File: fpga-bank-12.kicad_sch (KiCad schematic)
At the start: 1 part

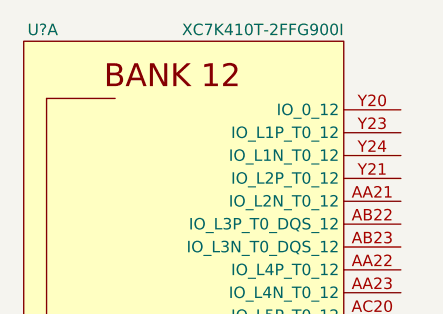
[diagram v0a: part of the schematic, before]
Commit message: Fix FPGA symbol
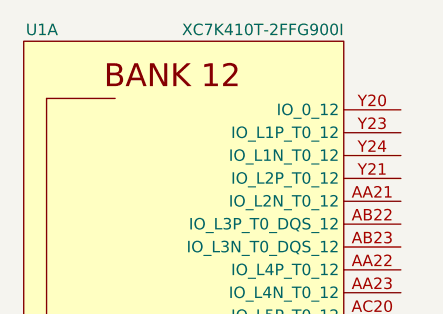
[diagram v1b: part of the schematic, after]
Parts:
- gave numbers to parts that had none: 1
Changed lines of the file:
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@@
     (effects (font (size 1.27 1.27)) (justify left))
   )
-  (symbol (lib_name "XC7K410T-2FFG900I_1") (lib_id "antmicroMicrocontrollers:XC7K410T-2FFG900I") (at 119.38 144.78 0) (unit 1)
+  (symbol (lib_id "antmicroMicrocontrollers:XC7K410T-2FFG900I") (at 119.38 144.78 0) (unit 1)
     (in_bom yes) (on_board yes)
-    (property "Reference" "U?" (id 0) (at 105.41 74.93 0)
+    (property "Reference" "U1" (id 0) (at 105.41 74.93 0)
       (effects (font (size 1.27 1.27)) (justify right))
     )

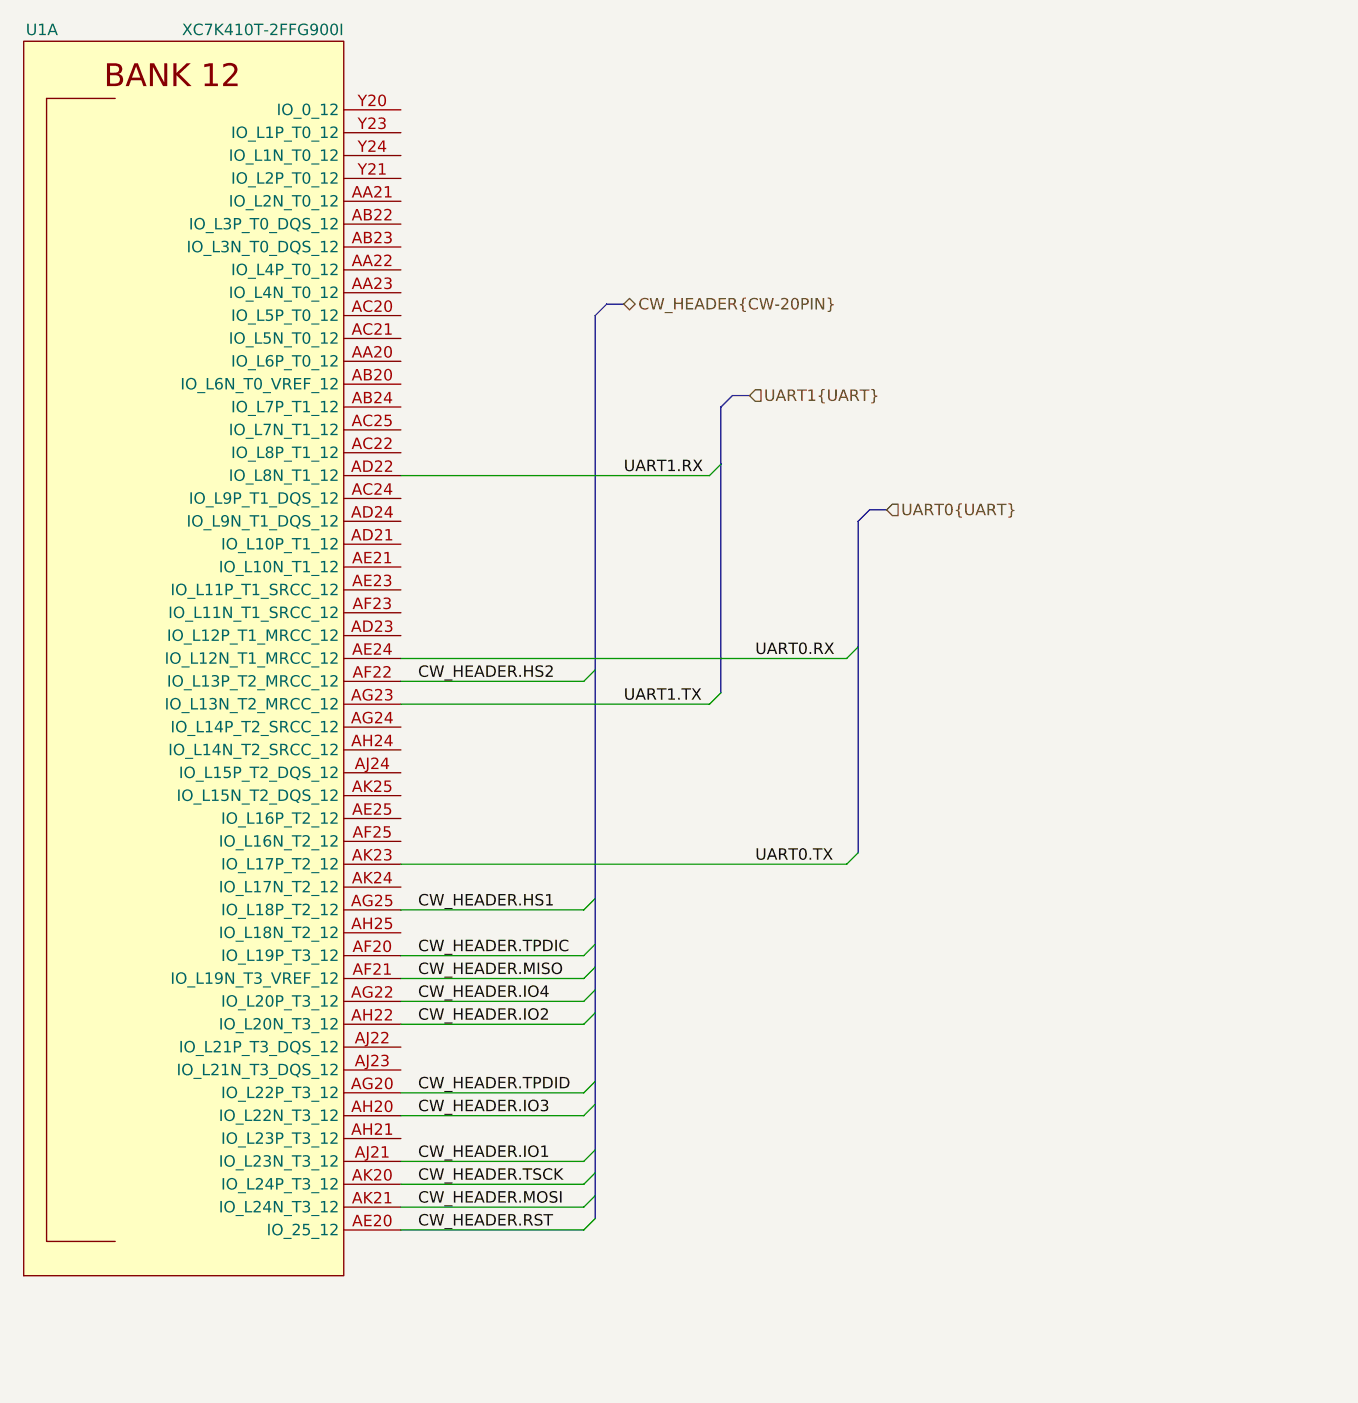
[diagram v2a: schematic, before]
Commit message: Add new pinout to sup MCU. Start connecting it to FPGA
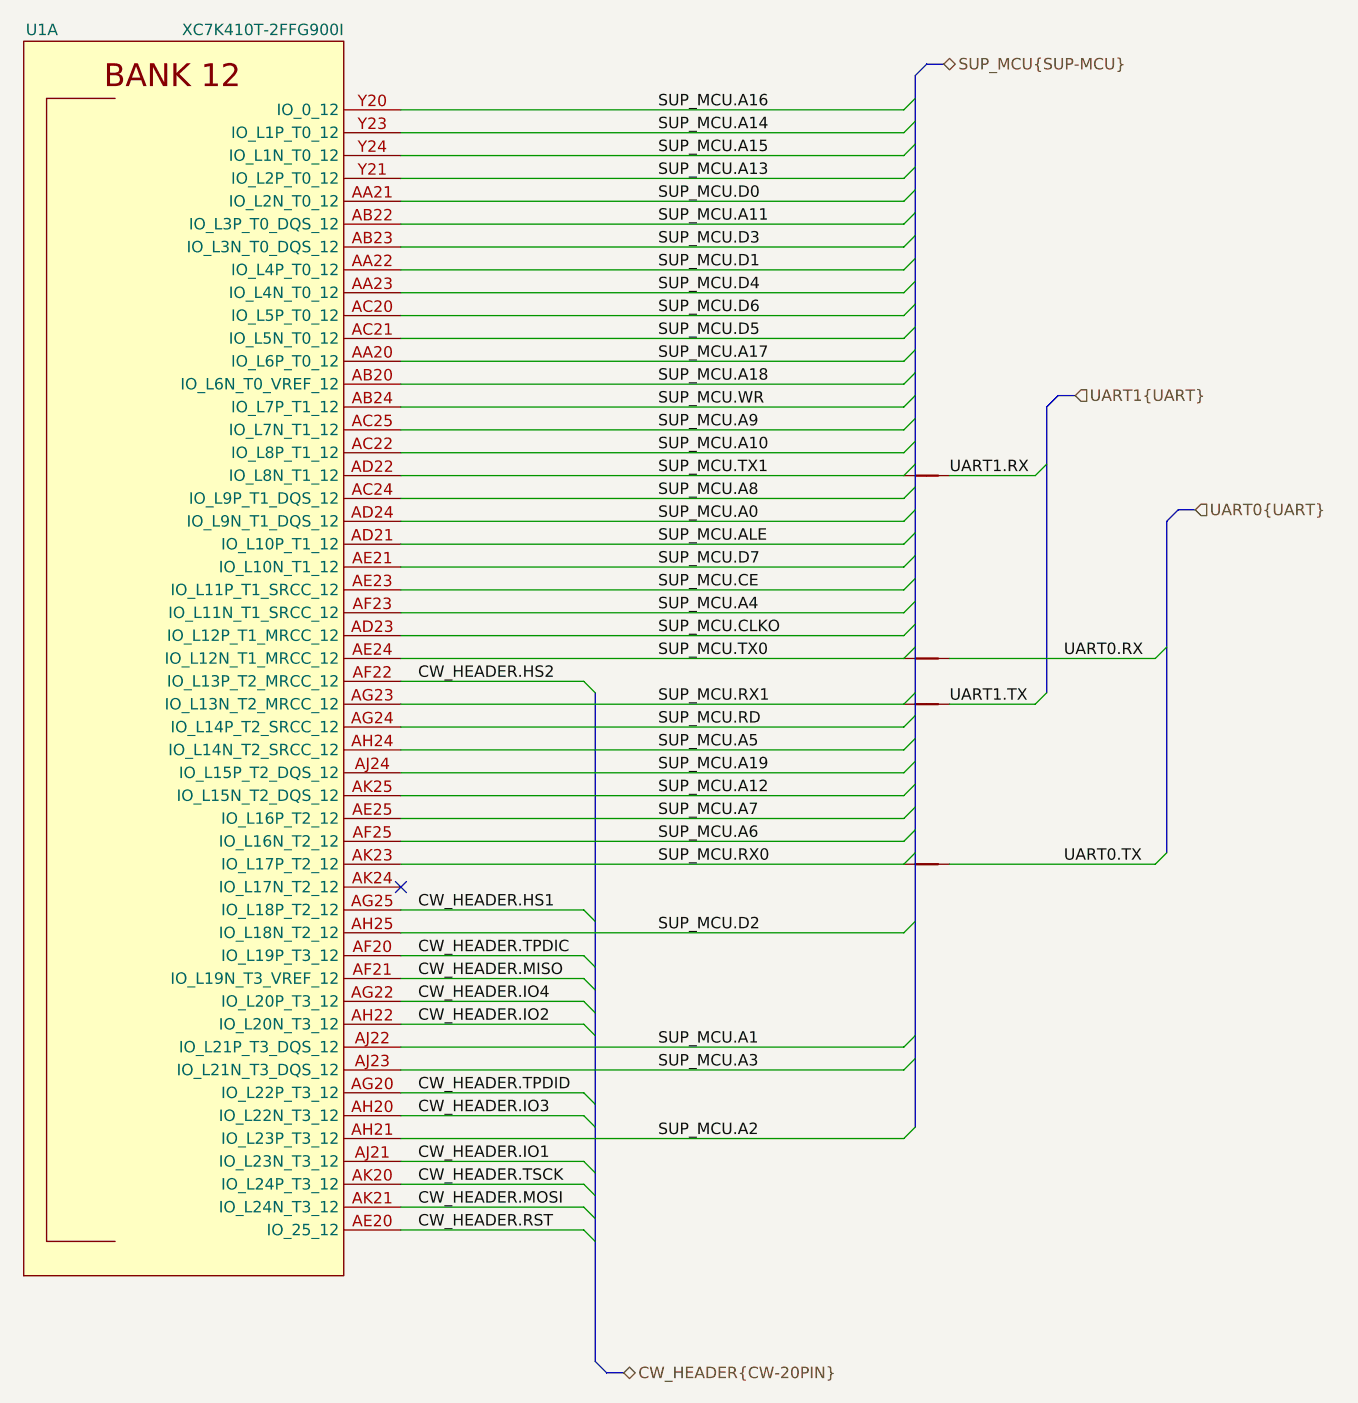
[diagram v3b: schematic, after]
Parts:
- added NT? (x4): NetTie_2, antmicro-footprints:NetTie-2_SMD_Pad0.127mm, symbol antmicroShuntsJumpers:NetTie_2
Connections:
- net UART0.RX: now also NT?.2; no longer U1.AE24 (IO_L12N_T1_MRCC_12)
- net UART0.TX: now also NT?.2; no longer U1.AK23 (IO_L17P_T2_12)
- net UART1.RX: now also NT?.2; no longer U1.AD22 (IO_L8N_T1_12)
- net UART1.TX: now also NT?.2; no longer U1.AG23 (IO_L13N_T2_MRCC_12)
- net SUP_MCU.A17: now reaches U1.AA20 (IO_L6P_T0_12)
- net SUP_MCU.D0: now reaches U1.AA21 (IO_L2N_T0_12)
- net SUP_MCU.D1: now reaches U1.AA22 (IO_L4P_T0_12)
- net SUP_MCU.D4: now reaches U1.AA23 (IO_L4N_T0_12)
- net SUP_MCU.A18: now reaches U1.AB20 (IO_L6N_T0_VREF_12)
- net SUP_MCU.A11: now reaches U1.AB22 (IO_L3P_T0_DQS_12)
- net SUP_MCU.D3: now reaches U1.AB23 (IO_L3N_T0_DQS_12)
- net SUP_MCU.WR: now reaches U1.AB24 (IO_L7P_T1_12)
- net SUP_MCU.D6: now reaches U1.AC20 (IO_L5P_T0_12)
- net SUP_MCU.D5: now reaches U1.AC21 (IO_L5N_T0_12)
- net SUP_MCU.A10: now reaches U1.AC22 (IO_L8P_T1_12)
- net SUP_MCU.A8: now reaches U1.AC24 (IO_L9P_T1_DQS_12)
- net SUP_MCU.A9: now reaches U1.AC25 (IO_L7N_T1_12)
- net SUP_MCU.ALE: now reaches U1.AD21 (IO_L10P_T1_12)
- net SUP_MCU.CLKO: now reaches U1.AD23 (IO_L12P_T1_MRCC_12)
- net SUP_MCU.A0: now reaches U1.AD24 (IO_L9N_T1_DQS_12)
- net SUP_MCU.D7: now reaches U1.AE21 (IO_L10N_T1_12)
- net SUP_MCU.CE: now reaches U1.AE23 (IO_L11P_T1_SRCC_12)
- net SUP_MCU.A7: now reaches U1.AE25 (IO_L16P_T2_12)
- net SUP_MCU.A4: now reaches U1.AF23 (IO_L11N_T1_SRCC_12)
- net SUP_MCU.A6: now reaches U1.AF25 (IO_L16N_T2_12)
- net SUP_MCU.RD: now reaches U1.AG24 (IO_L14P_T2_SRCC_12)
- net SUP_MCU.A2: now reaches U1.AH21 (IO_L23P_T3_12)
- net SUP_MCU.A5: now reaches U1.AH24 (IO_L14N_T2_SRCC_12)
- net SUP_MCU.D2: now reaches U1.AH25 (IO_L18N_T2_12)
- net SUP_MCU.A1: now reaches U1.AJ22 (IO_L21P_T3_DQS_12)
- net SUP_MCU.A3: now reaches U1.AJ23 (IO_L21N_T3_DQS_12)
- net SUP_MCU.A19: now reaches U1.AJ24 (IO_L15P_T2_DQS_12)
- net SUP_MCU.A12: now reaches U1.AK25 (IO_L15N_T2_DQS_12)
- net SUP_MCU.A16: now reaches U1.Y20 (IO_0_12)
- net SUP_MCU.A13: now reaches U1.Y21 (IO_L2P_T0_12)
- net SUP_MCU.A14: now reaches U1.Y23 (IO_L1P_T0_12)
- net SUP_MCU.A15: now reaches U1.Y24 (IO_L1N_T0_12)
- new net SUP_MCU.RX0: NT?.1, U1.AK23 (IO_L17P_T2_12)
- new net SUP_MCU.RX1: NT?.1, U1.AG23 (IO_L13N_T2_MRCC_12)
- new net SUP_MCU.TX0: NT?.1, U1.AE24 (IO_L12N_T1_MRCC_12)
- new net SUP_MCU.TX1: NT?.1, U1.AD22 (IO_L8N_T1_12)
- no-connect marks 0 -> 1

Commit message: Add DDR3L decoupling capacitors
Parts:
- gave numbers to parts that had none: 4
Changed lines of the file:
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@@
   (symbol (lib_id "antmicroShuntsJumpers:NetTie_2") (at 201.93 144.78 0) (unit 1)
     (in_bom yes) (on_board yes) (fields_autoplaced)
-    (property "Reference" "NT?" (id 0) (at 201.93 143.51 0)
+    (property "Reference" "NT16" (id 0) (at 201.93 143.51 0)
       (effects (font (size 1.27 1.27)) hide)
     )
@@
   (symbol (lib_id "antmicroShuntsJumpers:NetTie_2") (at 201.93 167.64 0) (unit 1)
     (in_bom yes) (on_board yes) (fields_autoplaced)
-    (property "Reference" "NT?" (id 0) (at 201.93 166.37 0)
+    (property "Reference" "NT18" (id 0) (at 201.93 166.37 0)
       (effects (font (size 1.27 1.27)) hide)
     )
@@
   (symbol (lib_id "antmicroShuntsJumpers:NetTie_2") (at 201.93 149.86 0) (unit 1)
     (in_bom yes) (on_board yes) (fields_autoplaced)
-    (property "Reference" "NT?" (id 0) (at 201.93 148.59 0)
+    (property "Reference" "NT17" (id 0) (at 201.93 148.59 0)
       (effects (font (size 1.27 1.27)) hide)
     )
@@
   (symbol (lib_id "antmicroShuntsJumpers:NetTie_2") (at 201.93 124.46 0) (unit 1)
     (in_bom yes) (on_board yes) (fields_autoplaced)
-    (property "Reference" "NT?" (id 0) (at 201.93 123.19 0)
-      (effects (font (size 1.27 1.27)) hide)
-    )
+    (property "Reference" "NT15" (id 0) (at 201.93 123.19 0)
+      (effects (font (size 1.27 1.27)) hide)
+    )

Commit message: Loclib
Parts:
- NT15, NT16, NT17, NT18: footprint antmicro-footprints:NetTie-2_SMD_Pad0.127mm -> K410T-devboard-footprints:NetTie-2_SMD_Pad0.127mm; symbol antmicroShuntsJumpers:NetTie_2 -> K410T-devboard:NetTie_2
- U1: footprint antmicro-footprints:xc7k410t-2ffg900I -> K410T-devboard-footprints:xc7k410t-2ffg900I; symbol antmicroMicrocontrollers:XC7K410T-2FFG900I -> K410T-devboard:XC7K410T-2FFG900I
